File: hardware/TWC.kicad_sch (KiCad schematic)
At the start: 44 parts, among them J1 Screw_Terminal_01x04, J2 Conn_02x05_Odd_Even, J3 Conn_02x05_Odd_Even, J4 Conn_01x10_Male, J6 Screw_Terminal_01x02, SW1 SW_Push, SW2 SW_Push, U1 MAX3485, U2 Si7021-A20, U3 TPS56339DDC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

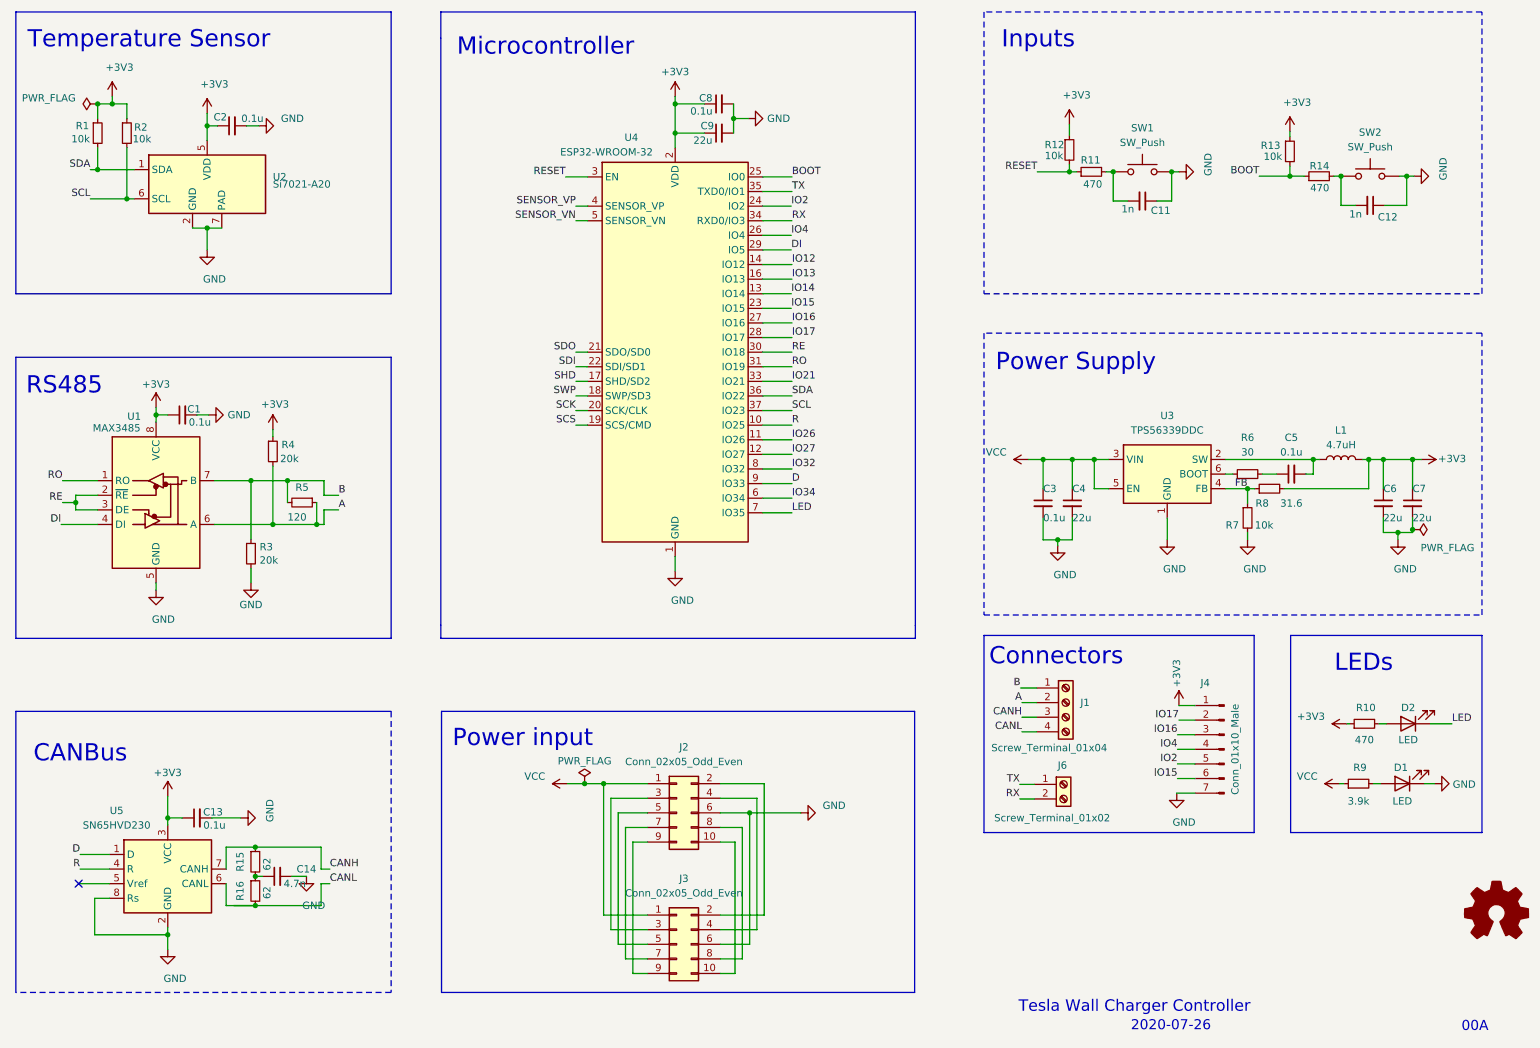
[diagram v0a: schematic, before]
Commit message: Many small updates, including changing the Buck Converter and temperature sensor to more available parts, changed the screw terminals to the final footprint (0.1" pitch)
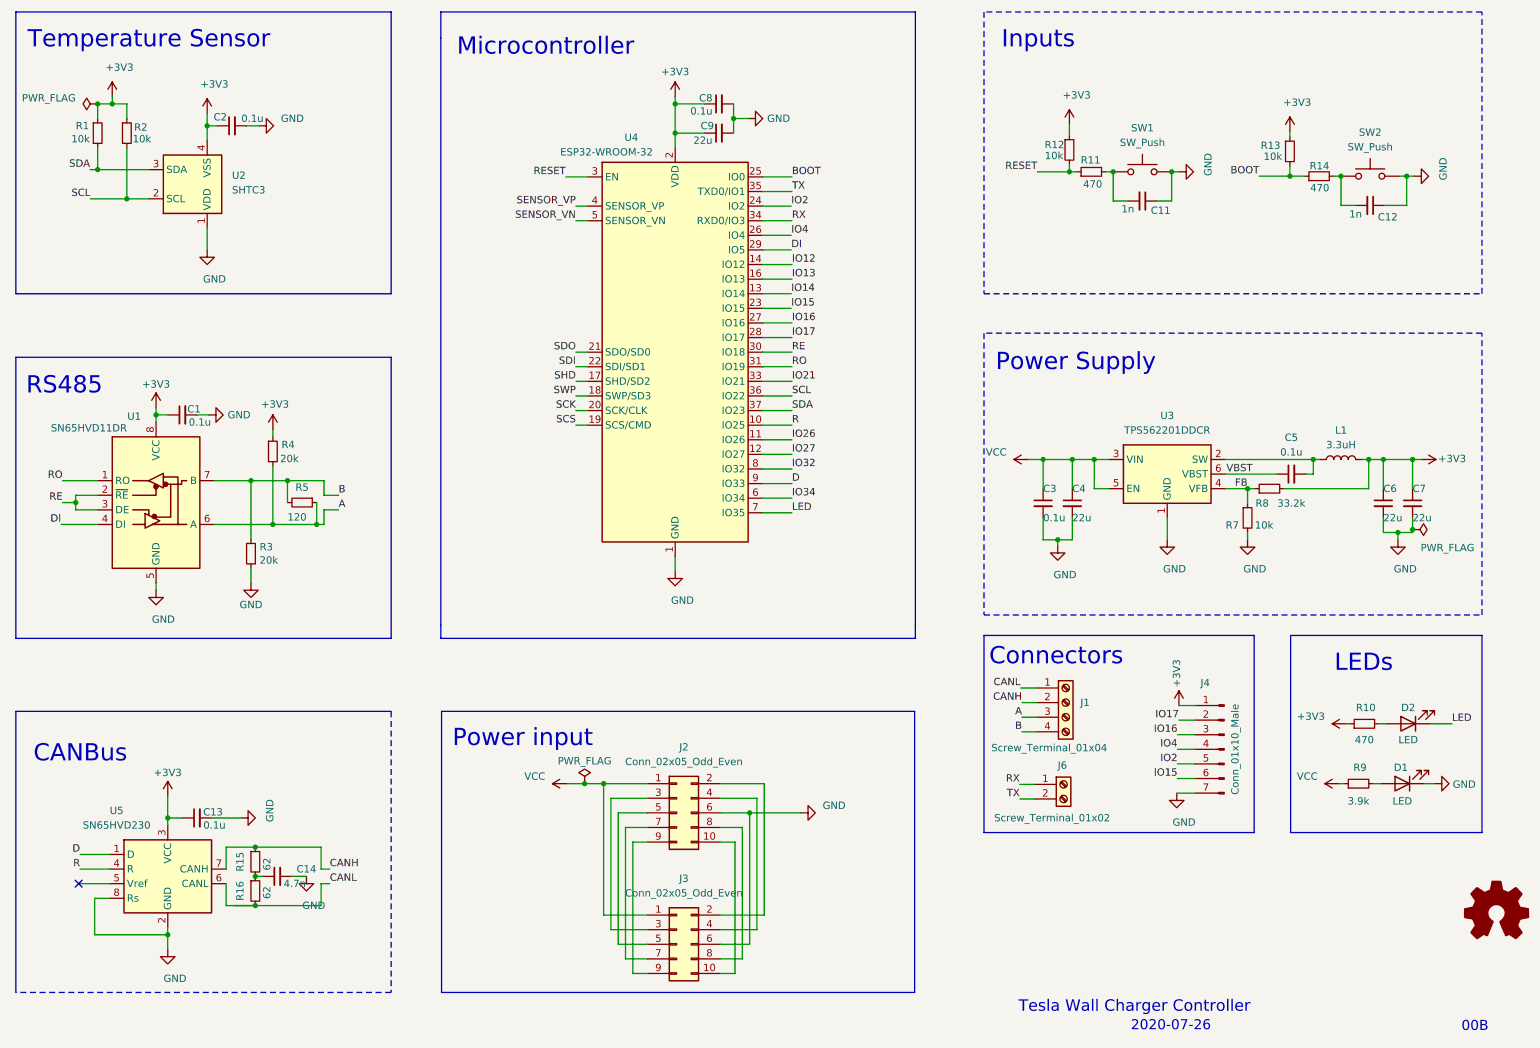
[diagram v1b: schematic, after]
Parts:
- removed R6: 30, Capacitor_SMD:C_0603_1608Metric, symbol Device:R_Small
- removed U2: Si7021-A20, Package_DFN_QFN:DFN-6-1EP_3x3mm_P1mm_EP1.5x2.4mm, symbol Sensor_Humidity:Si7021-A20
- added U2: SHTC3, Sensor_Humidity:Sensirion_DFN-4-1EP_2x2mm_P1mm_EP0.7x1.6mm, symbol Sensor_Humidity:SHTC3
- J1: footprint TerminalBlock_TE-Connectivity:TerminalBlock_TE_282834-4_1x04_P2.54mm_Horizontal -> TerminalBlock_Altech:Altech_AK500_1x04_P5.00
- J6: footprint TerminalBlock_TE-Connectivity:TerminalBlock_TE_282834-2_1x02_P2.54mm_Horizontal -> TerminalBlock_Altech:Altech_AK500_1x02_P5.00
- L1: value 4.7uH -> 3.3uH; footprint Inductor_SMD:L_Taiyo-Yuden_NR-40xx -> Inductor_SMD:L_Taiyo-Yuden_NR-30xx
- R1, R10, R11, R12, R13, R14, R2, R7, R9: footprint Capacitor_SMD:C_0603_1608Metric -> Resistor_SMD:R_0603_1608Metric
- R8: value 31.6 -> 33.2k; footprint Capacitor_SMD:C_0603_1608Metric -> Resistor_SMD:R_0603_1608Metric
- SW1, SW2: footprint Button_Switch_SMD:SW_SPST_CK_PTS636_SX25_XMTR_LFS -> Button_Switch_SMD:SW_SPST_TS_1101_X_X
- U1: value MAX3485 -> SN65HVD11DR
- U3: value TPS56339DDC -> TPS562201DDCR; symbol Regulator_Switching:TPS56339DDC -> Regulator_Switching:TPS562200
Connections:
- net +3V3: now also U2.4 (VSS)
- net A: now also J1.3 (Pin_3); no longer J1.2 (Pin_2)
- net B: now also J1.4 (Pin_4); no longer J1.1 (Pin_1)
- net CANH: now also J1.2 (Pin_2); no longer J1.3 (Pin_3)
- net CANL: now also J1.1 (Pin_1); no longer J1.4 (Pin_4)
- net GND: now also U2.1 (VDD)
- net RX: now also J6.1 (Pin_1); no longer J6.2 (Pin_2)
- net SCL: now also U4.36 (IO22), U2.2 (SCL); no longer U4.37 (IO23)
- net SDA: now also U4.37 (IO23), U2.3 (SDA); no longer U4.36 (IO22)
- net TX: now also J6.2 (Pin_2); no longer J6.1 (Pin_1)
- net VBST: now reaches U3.6 (VBST)
- net VBST: now also C5.1
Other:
- note added: "00B"
- note removed: "00A"

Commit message: Revision 00B with added logos, small cosmetic fixes
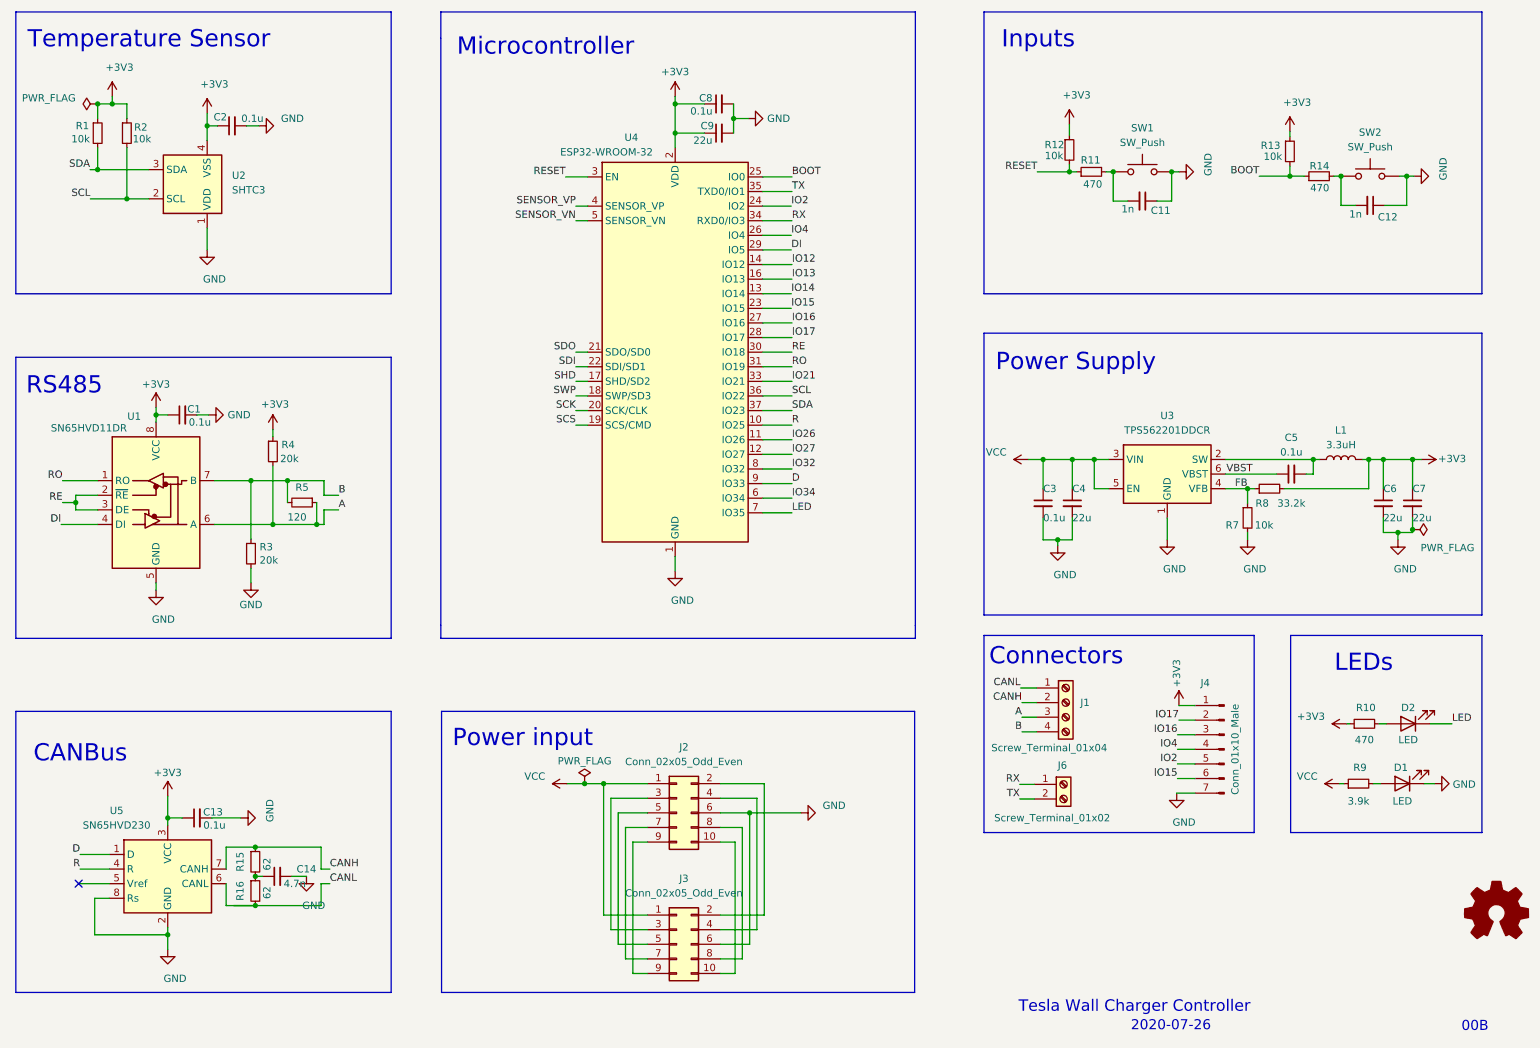
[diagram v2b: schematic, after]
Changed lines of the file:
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@@
   )
   (polyline (pts (xy 82.296 138.938) (xy 82.296 187.833))
-    (stroke (width 0.152) (type dash) (color 0 0 0 0))
+    (stroke (width 0.152) (type solid) (color 0 0 0 0))
   )
   (polyline (pts (xy 82.296 187.833) (xy 17.018 187.833))
-    (stroke (width 0.152) (type dash) (color 0 0 0 0))
+    (stroke (width 0.152) (type solid) (color 0 0 0 0))
   )
   (polyline (pts (xy 90.932 17.272) (xy 90.932 21.844))
@@
   )
   (polyline (pts (xy 185.42 17.272) (xy 185.42 66.294))
-    (stroke (width 0.152) (type dash) (color 0 0 0 0))
+    (stroke (width 0.152) (type solid) (color 0 0 0 0))
   )
   (polyline (pts (xy 185.42 66.294) (xy 272.034 66.294))
-    (stroke (width 0.152) (type dash) (color 0 0 0 0))
+    (stroke (width 0.152) (type solid) (color 0 0 0 0))
   )
   (polyline (pts (xy 185.42 73.152) (xy 185.42 122.174))
-    (stroke (width 0.152) (type dash) (color 0 0 0 0))
+    (stroke (width 0.152) (type solid) (color 0 0 0 0))
   )
   (polyline (pts (xy 185.42 122.174) (xy 272.034 122.174))
-    (stroke (width 0.152) (type dash) (color 0 0 0 0))
+    (stroke (width 0.152) (type solid) (color 0 0 0 0))
   )
   (polyline (pts (xy 185.42 125.73) (xy 185.42 160.02))
@@
   )
   (polyline (pts (xy 272.034 17.272) (xy 185.42 17.272))
-    (stroke (width 0.152) (type dash) (color 0 0 0 0))
+    (stroke (width 0.152) (type solid) (color 0 0 0 0))
   )
   (polyline (pts (xy 272.034 66.294) (xy 272.034 17.272))
-    (stroke (width 0.152) (type dash) (color 0 0 0 0))
+    (stroke (width 0.152) (type solid) (color 0 0 0 0))
   )
   (polyline (pts (xy 272.034 73.152) (xy 185.42 73.152))
-    (stroke (width 0.152) (type dash) (color 0 0 0 0))
+    (stroke (width 0.152) (type solid) (color 0 0 0 0))
   )
   (polyline (pts (xy 272.034 122.174) (xy 272.034 73.152))
-    (stroke (width 0.152) (type dash) (color 0 0 0 0))
+    (stroke (width 0.152) (type solid) (color 0 0 0 0))
   )
   (polyline (pts (xy 272.034 160.02) (xy 272.034 125.73))
